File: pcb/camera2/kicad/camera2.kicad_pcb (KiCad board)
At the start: 4 copper layers, 96.5 x 45.7 mm, 71 parts

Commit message: DRC passes
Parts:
- removed the B10C at (146.4, 92.6)
- removed the B11C at (149.6, 72.3)
- removed the B15C at (153.1, 72.3)
- removed the B16C at (152.5, 67.3)
- removed the B17C at (164.4, 92.7)
- removed the B18C at (146.4, 67.3)
- removed the B19C at (166.1, 88.5)
- removed the B1C at (120.0, 88.3)
- removed the B20C at (149.9, 70.8)
- removed the B2C at (132.8, 91.7)
- removed the B3C at (153.3, 70.7)
- removed the B4C at (156.6, 70.3)
- removed the B5C at (146.5, 69.0)
- removed the B6C at (146.1, 70.5)
- removed D0C, D1C, D2C, D3C, L0, L1, L2, L3, U3C: , gen:14fdd466f7178f17380f48cf89da463f18b4a0e8fcfb609cb3e620722c947cd3
- removed D0R, D1R, D2R, D3R, RT: , gen:57f8f96f6e6b2a00af4539d585b2f3bdc0d73935af5ecd13a4a5208aab3df262
- removed U3: , gen:7dbf8df50efd715a448db095119b3b26608df54065546b11197adccbe633bb61
- added B10C: , gen:b8abd8cbc0b572999067c05d37fd407a90732e005a9769bc0f5d9b36d5f7537a, B.Cu at (146.4, 92.6)
- added B11C: , gen:b8abd8cbc0b572999067c05d37fd407a90732e005a9769bc0f5d9b36d5f7537a, B.Cu at (155.3, 91.9)
- added B15C: , gen:b8abd8cbc0b572999067c05d37fd407a90732e005a9769bc0f5d9b36d5f7537a, B.Cu at (164.1, 98.0)
- added B16C: , gen:b8abd8cbc0b572999067c05d37fd407a90732e005a9769bc0f5d9b36d5f7537a, B.Cu at (160.0, 91.0)
- added B17C: , gen:b8abd8cbc0b572999067c05d37fd407a90732e005a9769bc0f5d9b36d5f7537a, B.Cu at (164.4, 92.7)
- added B18C: , gen:b8abd8cbc0b572999067c05d37fd407a90732e005a9769bc0f5d9b36d5f7537a, B.Cu at (161.6, 86.6)
- added B19C: , gen:b8abd8cbc0b572999067c05d37fd407a90732e005a9769bc0f5d9b36d5f7537a, B.Cu at (166.1, 88.5)
- added B1C: , gen:b8abd8cbc0b572999067c05d37fd407a90732e005a9769bc0f5d9b36d5f7537a, B.Cu at (120.0, 88.3)
- added B20C: , gen:b8abd8cbc0b572999067c05d37fd407a90732e005a9769bc0f5d9b36d5f7537a, B.Cu at (180.7, 89.4)
- added B2C: , gen:b8abd8cbc0b572999067c05d37fd407a90732e005a9769bc0f5d9b36d5f7537a, B.Cu at (134.7, 90.3)
- added B3C: , gen:b8abd8cbc0b572999067c05d37fd407a90732e005a9769bc0f5d9b36d5f7537a, B.Cu at (140.1, 87.0)
- added B4C: , gen:b8abd8cbc0b572999067c05d37fd407a90732e005a9769bc0f5d9b36d5f7537a, B.Cu at (137.4, 93.0)
- added B5C: , gen:b8abd8cbc0b572999067c05d37fd407a90732e005a9769bc0f5d9b36d5f7537a, B.Cu at (142.8, 89.9)
- added B6C: , gen:b8abd8cbc0b572999067c05d37fd407a90732e005a9769bc0f5d9b36d5f7537a, B.Cu at (140.2, 95.8)
- added ID0C: , gen:b8abd8cbc0b572999067c05d37fd407a90732e005a9769bc0f5d9b36d5f7537a, B.Cu at (147.1, 118.2)
- added ID0R: , gen:8b8e8cdd2a6c07e3e6c854f6b6a8f0d2287e4fa4909b824e776fd2ffcb4b4dd2, F.Cu at (150.7, 118.2)
- added ID1C: , gen:b8abd8cbc0b572999067c05d37fd407a90732e005a9769bc0f5d9b36d5f7537a, B.Cu at (147.3, 119.2)
- added ID1R: , gen:8b8e8cdd2a6c07e3e6c854f6b6a8f0d2287e4fa4909b824e776fd2ffcb4b4dd2, F.Cu at (150.8, 119.2)
- added ID2C: , gen:b8abd8cbc0b572999067c05d37fd407a90732e005a9769bc0f5d9b36d5f7537a, B.Cu at (147.1, 120.2)
- added ID2R: , gen:8b8e8cdd2a6c07e3e6c854f6b6a8f0d2287e4fa4909b824e776fd2ffcb4b4dd2, F.Cu at (150.9, 120.3)
- added ID3C: , gen:b8abd8cbc0b572999067c05d37fd407a90732e005a9769bc0f5d9b36d5f7537a, B.Cu at (147.3, 121.1)
- added ID3R: , gen:8b8e8cdd2a6c07e3e6c854f6b6a8f0d2287e4fa4909b824e776fd2ffcb4b4dd2, F.Cu at (150.9, 121.4)
- added ID4C: , gen:b8abd8cbc0b572999067c05d37fd407a90732e005a9769bc0f5d9b36d5f7537a, F.Cu at (155.4, 118.0)
- added ID5C: , gen:b8abd8cbc0b572999067c05d37fd407a90732e005a9769bc0f5d9b36d5f7537a, F.Cu at (155.3, 119.1)
- added ID6C: , gen:b8abd8cbc0b572999067c05d37fd407a90732e005a9769bc0f5d9b36d5f7537a, F.Cu at (155.5, 120.2)
- added ID7C: , gen:b8abd8cbc0b572999067c05d37fd407a90732e005a9769bc0f5d9b36d5f7537a, F.Cu at (155.5, 121.3)
- added IL0: , gen:5ee2e2daf856c7b57c8b813aab30cc4a712b0ba6b927f36d7f82f0d8799f116d, B.Cu at (149.8, 116.5)
- added IL1: , gen:5ee2e2daf856c7b57c8b813aab30cc4a712b0ba6b927f36d7f82f0d8799f116d, B.Cu at (150.8, 116.5)
- added IL2: , gen:5ee2e2daf856c7b57c8b813aab30cc4a712b0ba6b927f36d7f82f0d8799f116d, B.Cu at (151.9, 116.5)
- added IL3: , gen:5ee2e2daf856c7b57c8b813aab30cc4a712b0ba6b927f36d7f82f0d8799f116d, B.Cu at (153.0, 116.5)
- added IR1: , gen:8b8e8cdd2a6c07e3e6c854f6b6a8f0d2287e4fa4909b824e776fd2ffcb4b4dd2, F.Cu at (159.0, 112.3)
- added IR2: , gen:8b8e8cdd2a6c07e3e6c854f6b6a8f0d2287e4fa4909b824e776fd2ffcb4b4dd2, F.Cu at (159.2, 114.0)
- added IRT: , gen:8b8e8cdd2a6c07e3e6c854f6b6a8f0d2287e4fa4909b824e776fd2ffcb4b4dd2, B.Cu at (151.1, 107.4)
- added IU3: , gen:72d1805f8915362f91f0e14214fca19b3aed8f32e64a953ec1b58a37910379a2, B.Cu at (151.4, 111.9)
- added IU3C: , gen:b8abd8cbc0b572999067c05d37fd407a90732e005a9769bc0f5d9b36d5f7537a, B.Cu at (145.8, 113.0)
- B1, B10, B11, B15, B16, B17, B18, B19, B2, B20, B3, B4, B5, B6: footprint gen:b84940fdfb16a2d7942b3b406dd98b10c2c2213999c6866e353299b244b8fc6e -> gen:bff32cade4af0a95ca028e7527e650a4e6c1ba088b705a33382b7ae8c82c305d
- C1: footprint gen:576178f3c780c7e887b8d2770ad844677200359bd7336c4d76e786b1bd821a08 -> gen:b8abd8cbc0b572999067c05d37fd407a90732e005a9769bc0f5d9b36d5f7537a
- C1M1, C2M1: footprint gen:65e19b3f16ad4d4d8558c7978771f760d319ed626d2efc1485c23fcec7e6c7b6 -> gen:4d59d39d10787b911058ae9333354a532030edea4cb4e53179d64fabcbdb6f99
- C1R1, C1R2, C2R1, C2R2, R2: footprint gen:57f8f96f6e6b2a00af4539d585b2f3bdc0d73935af5ecd13a4a5208aab3df262 -> gen:8b8e8cdd2a6c07e3e6c854f6b6a8f0d2287e4fa4909b824e776fd2ffcb4b4dd2
- C1U1, C2U1: footprint gen:d5f9e289ee2336b21afcfae927cf410e4925b1050bf518abb5cf178e2b219273 -> gen:2784497294436a743af50a5d521ce1181bd153dedc4157f9addccb1934030dc3
- C2: footprint gen:14fdd466f7178f17380f48cf89da463f18b4a0e8fcfb609cb3e620722c947cd3 -> gen:96d8d9f3b01e3a213437eecc57d99723256313ff0fc11d8291488d1af641475f
- P1: footprint gen:3c3694fa26875b1e02c9ec8a97da8ee5419b5448db42b56d2f0a8391397f0416 -> gen:3f8ed9d7be0e74029e88378a59fbf78c1191c3dbd4709bec51884f93e57b519c
- REG0: footprint gen:1add349ebd9963d752faf6d62c14ce67e4cb2b1431c56764e8a0fc8115b29539 -> gen:33f05abcc9f1c63f6620fa979925c1be2170a0d935dd6266c3361443b1a0b93c
- REG1: footprint gen:301270a8d4f2b83b7524f9f1e316186f15d4407ffff898fc97f7a9bf814ba95e -> gen:19207bd7838306c4c523d784bf9550b872fb808274892b7f9326e1c601df3f52
- REG2: footprint gen:3dff63c1257816c390bd930d4e9e2a3d002c3804d7440e0068ce39245183ded9 -> gen:d2318dfe08ea0e31695b166a9aadcf0dc3f3257fb96d848578f4303faa6cf295
- REG3: footprint gen:fab45f821aaed4b2e2c106769317244450312030644283560206288729765279 -> gen:349ed32a726ad85c4c2a09d1be6ab027e3173327b7b9892fb1b4a9c1a6d5effb
- U1: footprint gen:0306e6b5f641219b29c97fb93a4bb6fb11c91cc1b6f63197c18a4913509fb757 -> gen:07f267ebbbba037e2ec6e358fcf8ea4347767a42bf146607db79b5699d1f6bbc
- U2: footprint gen:2b1b8886a1ea8f37823178f4470ad8a0f26e8cdd6924e7ac0c0e142e2d1baa6b -> gen:37c349b4ccef9ca1e6dfa7e726c437006c67516ca70700a0b276a014844c8cb2
- moved C1 7.46 mm to (212.7, 90.4)
- moved B15 5.05 mm to (165.6, 101.0)
- moved B16 2.42 mm to (161.7, 94.2)
- moved REG3 0.45 mm to (161.6, 119.3)
- moved REG1 0.41 mm to (141.4, 119.7)
- moved REG2 0.34 mm to (162.0, 104.4)
- renumbered D0 to ID0, D1 to ID1, D2 to ID2, D3 to ID3
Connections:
- net B10_1_NC renamed _B10_1_NC
- net B10_4_NC renamed _B10_4_NC
- net B10_5_NC renamed _B10_5_NC
- net B11_1_NC renamed _B11_1_NC
- net B11_4_NC renamed _B11_4_NC
- net B11_5_NC renamed _B11_5_NC
- net B15_1_NC renamed _B15_1_NC
- net B15_4_NC renamed _B15_4_NC
- net B15_5_NC renamed _B15_5_NC
- net B16_1_NC renamed _B16_1_NC
- net B16_4_NC renamed _B16_4_NC
- net B16_5_NC renamed _B16_5_NC
- net B17_1_NC renamed _B17_1_NC
- net B17_4_NC renamed _B17_4_NC
- net B17_5_NC renamed _B17_5_NC
- net B18_1_NC renamed _B18_1_NC
- net B18_4_NC renamed _B18_4_NC
- net B18_5_NC renamed _B18_5_NC
- net B19_1_NC renamed _B19_1_NC
- net B19_4_NC renamed _B19_4_NC
- net B19_5_NC renamed _B19_5_NC
- net B1_1_NC renamed _B1_1_NC
- net B1_4_NC renamed _B1_4_NC
- net B1_5_NC renamed _B1_5_NC
- net B20_1_NC renamed _B20_1_NC
- net B20_4_NC renamed _B20_4_NC
- net B20_5_NC renamed _B20_5_NC
- net B2_1_NC renamed _B2_1_NC
- net B2_4_NC renamed _B2_4_NC
- net B2_5_NC renamed _B2_5_NC
- net B3_1_NC renamed _B3_1_NC
- net B3_4_NC renamed _B3_4_NC
- net B3_5_NC renamed _B3_5_NC
- net B4_1_NC renamed _B4_1_NC
- net B4_4_NC renamed _B4_4_NC
- net B4_5_NC renamed _B4_5_NC
- net B5_1_NC renamed _B5_1_NC
- net B5_4_NC renamed _B5_4_NC
- net B5_5_NC renamed _B5_5_NC
- net B6_1_NC renamed _B6_1_NC
- net B6_4_NC renamed _B6_4_NC
- net B6_5_NC renamed _B6_5_NC
- net REG0_4_NC renamed _REG0_4_NC
- net REG1_4_NC renamed _REG1_4_NC
- net REG2_4_NC renamed _REG2_4_NC
- net REG3_4_NC renamed _REG3_4_NC
- net T1U_17_NC renamed _T1U_17_NC
- net T1U_28_MIPI_CLK_N renamed _T1U_28_MIPI_CLK_N
- net T1U_29_MIPI_CLK_P renamed _T1U_29_MIPI_CLK_P
- net T1U_2_GPIO3 renamed _T1U_2_GPIO3
- net T1U_31_MIPI_DATA_N renamed _T1U_31_MIPI_DATA_N
- net T1U_32_MIPI_DATA_P renamed _T1U_32_MIPI_DATA_P
- net T1U_3_GPIO2 renamed _T1U_3_GPIO2
- net T1U_4_GPIO1 renamed _T1U_4_GPIO1
- net T1U_5_GPIO0 renamed _T1U_5_GPIO0
- net T2U_17_NC renamed _T2U_17_NC
- net T2U_28_MIPI_CLK_N renamed _T2U_28_MIPI_CLK_N
- net T2U_29_MIPI_CLK_P renamed _T2U_29_MIPI_CLK_P
- net T2U_2_GPIO3 renamed _T2U_2_GPIO3
- net T2U_31_MIPI_DATA_N renamed _T2U_31_MIPI_DATA_N
- net T2U_32_MIPI_DATA_P renamed _T2U_32_MIPI_DATA_P
- net T2U_3_GPIO2 renamed _T2U_3_GPIO2
- net T2U_4_GPIO1 renamed _T2U_4_GPIO1
- net T2U_5_GPIO0 renamed _T2U_5_GPIO0
- net U1_10_PA3 renamed _U1_10_PA3
- net U1_11_PA4 renamed _U1_11_PA4
- net U1_12_PA5 renamed _U1_12_PA5
- net U1_13_PA6 renamed _U1_13_PA6
- net U1_14_PA7 renamed _U1_14_PA7
- net U1_15_PB0 renamed _U1_15_PB0
- net U1_16_PB1 renamed _U1_16_PB1
- net U1_17_PB2 renamed _U1_17_PB2
- net U1_20_PA8 renamed _U1_20_PA8
- net U1_21_PA9 renamed _U1_21_PA9
- net U1_22_PA10 renamed _U1_22_PA10
- net U1_23_PA11 renamed _U1_23_PA11
- net U1_24_PA12 renamed _U1_24_PA12
- net U1_2_PD0 renamed _U1_2_PD0
- net U1_32_PB5 renamed _U1_32_PB5
- net U1_33_PB6 renamed _U1_33_PB6
- net U1_34_PB7 renamed _U1_34_PB7
- net U1_3_PD1 renamed _U1_3_PD1
- net U1_5_VSSA renamed _U1_5_VSSA
- net U1_6_VDDA renamed _U1_6_VDDA
- net U1_7_PA0 renamed _U1_7_PA0
- net U1_8_PA1 renamed _U1_8_PA1
- net U1_9_PA2 renamed _U1_9_PA2
- net U2_10_IO2_10 renamed _U2_10_IO2_10
- net U2_11_IO2_11 renamed _U2_11_IO2_11
- net U2_1_IO2_1 renamed _U2_1_IO2_1
- net U2_2_IO2_2 renamed _U2_2_IO2_2
- net U2_3_IO2_3 renamed _U2_3_IO2_3
- net U2_4_IO2_4 renamed _U2_4_IO2_4
- net U2_53_IO1_53 renamed _U2_53_IO1_53
- net U2_54_IO1_54 renamed _U2_54_IO1_54
- net U2_55_IO1_55 renamed _U2_55_IO1_55
- net U2_56_IO1_56 renamed _U2_56_IO1_56
- net U2_58_IO1_58 renamed _U2_58_IO1_58
- net U2_59_IO1_59 renamed _U2_59_IO1_59
- net U2_60_IO1_60 renamed _U2_60_IO1_60
- net U2_61_IO1_61 renamed _U2_61_IO1_61
- net U2_63_IO1_63 renamed _U2_63_IO1_63
- net U2_64_IO1_64 renamed _U2_64_IO1_64
- net U2_65_IO2_65 renamed _U2_65_IO2_65
- net U2_66_IO2_66 renamed _U2_66_IO2_66
- net U2_67_IO2_67 renamed _U2_67_IO2_67
- net U2_68_IO2_68 renamed _U2_68_IO2_68
- net U2_6_IO2_6 renamed _U2_6_IO2_6
- net U2_70_IO2_70 renamed _U2_70_IO2_70
- net U2_71_IO2_71 renamed _U2_71_IO2_71
- net U2_72_IO2_72 renamed _U2_72_IO2_72
- net U2_73_IO2_73 renamed _U2_73_IO2_73
- net U2_74_IO2_74 renamed _U2_74_IO2_74
- net U2_76_IO2_76 renamed _U2_76_IO2_76
- net U2_7_IO2_7 renamed _U2_7_IO2_7
- net U2_8_IO2_8 renamed _U2_8_IO2_8
- net U2_9_IO2_9 renamed _U2_9_IO2_9
- ID0 pad 1: cat0 -> Icat0
- ID0 pad 2: led0 -> Iled0
- ID1 pad 1: cat1 -> Icat1
- ID1 pad 2: led1 -> Iled1
- ID2 pad 1: cat2 -> Icat2
- ID2 pad 2: led2 -> Iled2
- ID3 pad 1: cat3 -> Icat3
- ID3 pad 2: led3 -> Iled3
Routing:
- net vcc3_0: track 4.31 -> 14.1 mm, vias 5 -> 14
- net gnd: track 30.7 -> 39.5 mm, vias 31 -> 43
- net pair15P: track 14.2 -> 19.3 mm
- net pair15N: track 17.2 -> 22.3 mm
- net out15P: track 30.7 -> 25.7 mm
- net out15N: track 31.0 -> 26.0 mm
- net vcc1_8: track 2.17 -> 5.21 mm, vias 2 -> 5
- net pair16N: track 10.8 -> 13.2 mm
- net pair16P: track 7.80 -> 10.3 mm
- net out16P: track 34.3 -> 31.9 mm
- net out16N: track 34.6 -> 32.2 mm
- net vcc3_3in: track 6.71 -> 6.12 mm, vias 2 -> 1
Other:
- rule pad_to_mask_clearance: 0.2 -> 0
- board text added: "1.8"

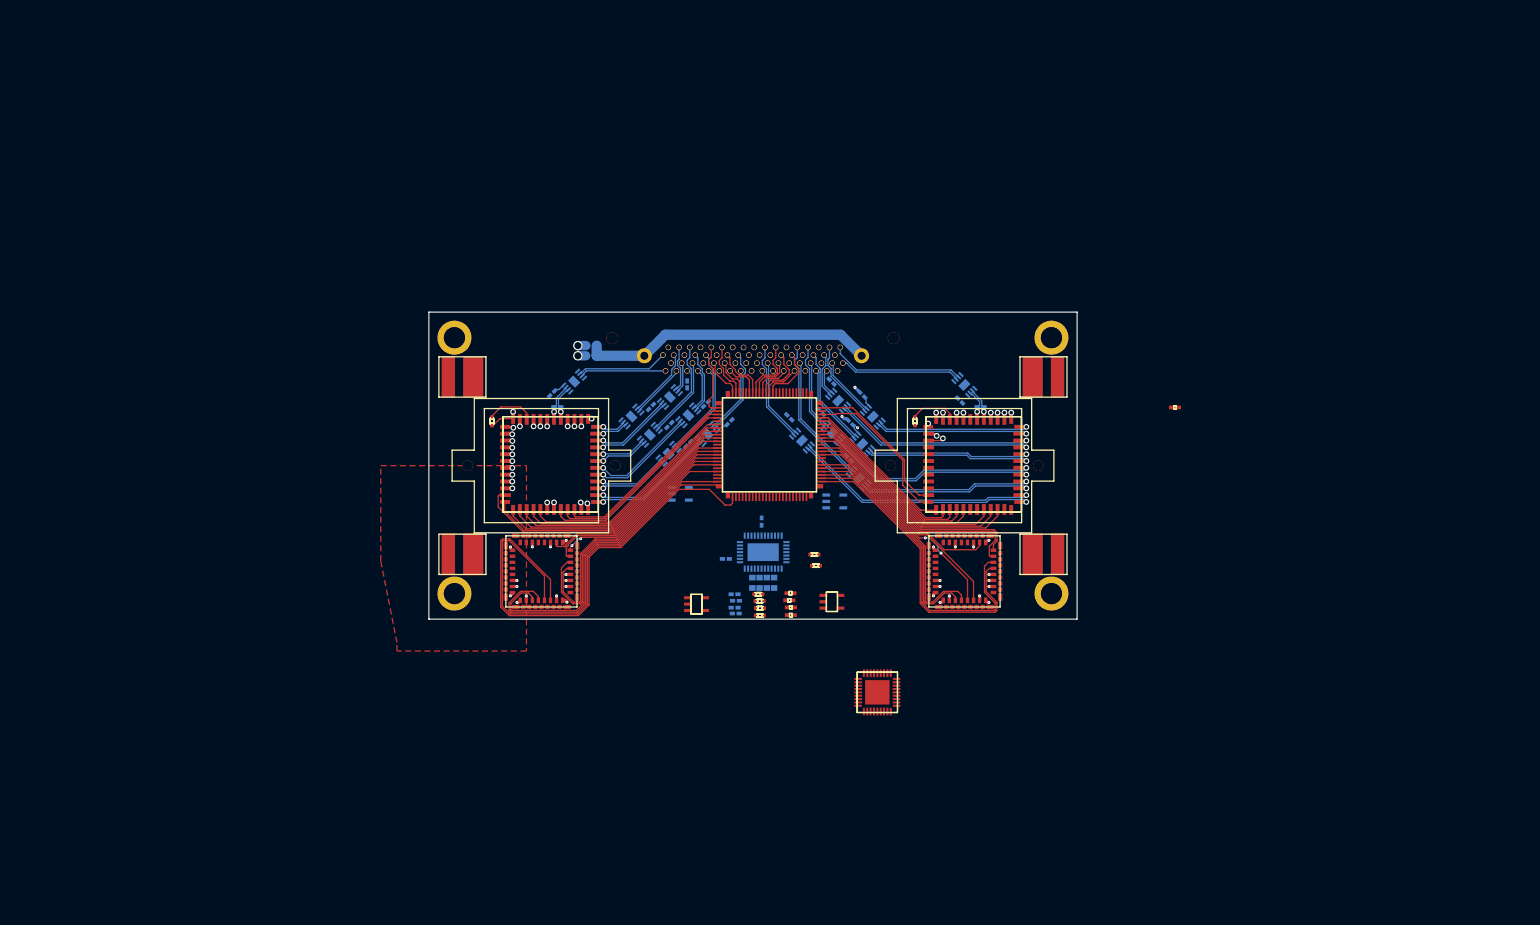
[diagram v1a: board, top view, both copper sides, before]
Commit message: adding decoupling capacitors
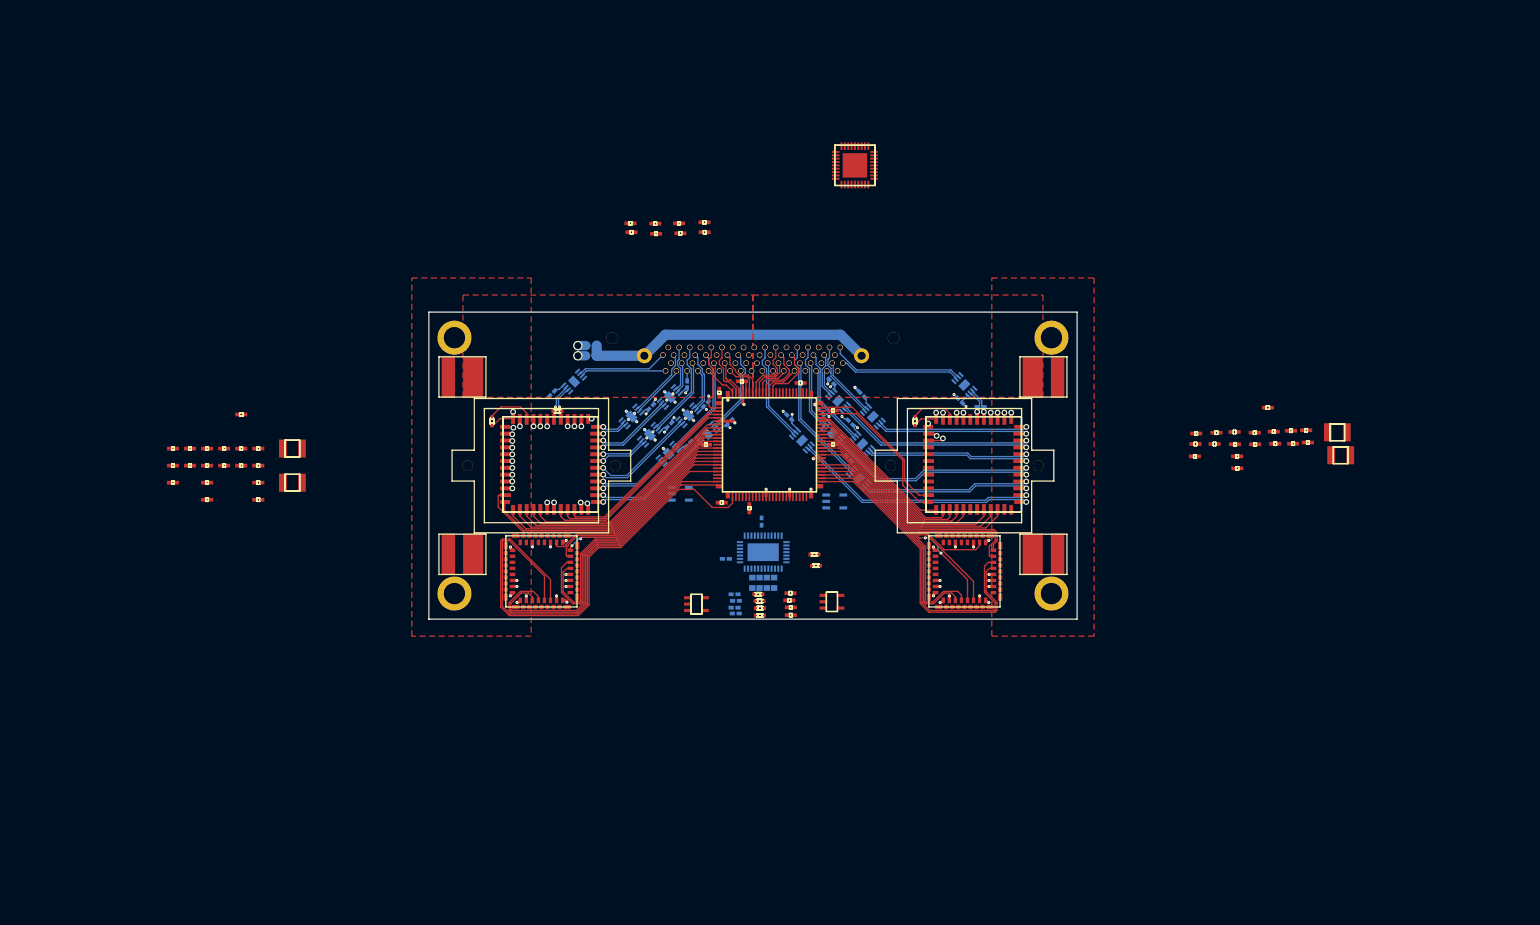
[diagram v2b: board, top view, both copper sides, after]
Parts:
- removed C1: , gen:b8abd8cbc0b572999067c05d37fd407a90732e005a9769bc0f5d9b36d5f7537a
- removed U1: , gen:07f267ebbbba037e2ec6e358fcf8ea4347767a42bf146607db79b5699d1f6bbc
- added C1C10: , gen:b8abd8cbc0b572999067c05d37fd407a90732e005a9769bc0f5d9b36d5f7537a, F.Cu at (63.5, 96.5)
- added C1C11: , gen:b8abd8cbc0b572999067c05d37fd407a90732e005a9769bc0f5d9b36d5f7537a, F.Cu at (63.5, 99.1)
- added C1C12: , gen:b8abd8cbc0b572999067c05d37fd407a90732e005a9769bc0f5d9b36d5f7537a, F.Cu at (63.5, 101.6)
- added C1C20: , gen:b8abd8cbc0b572999067c05d37fd407a90732e005a9769bc0f5d9b36d5f7537a, F.Cu at (66.0, 96.5)
- added C1C21: , gen:b8abd8cbc0b572999067c05d37fd407a90732e005a9769bc0f5d9b36d5f7537a, F.Cu at (66.0, 99.1)
- added C1C30: , gen:b8abd8cbc0b572999067c05d37fd407a90732e005a9769bc0f5d9b36d5f7537a, F.Cu at (68.6, 96.5)
- added C1C31: , gen:b8abd8cbc0b572999067c05d37fd407a90732e005a9769bc0f5d9b36d5f7537a, F.Cu at (68.6, 99.1)
- added C1C32: , gen:b8abd8cbc0b572999067c05d37fd407a90732e005a9769bc0f5d9b36d5f7537a, F.Cu at (68.6, 101.6)
- added C1C33: , gen:b8abd8cbc0b572999067c05d37fd407a90732e005a9769bc0f5d9b36d5f7537a, F.Cu at (68.6, 104.1)
- added C1C40: , gen:b8abd8cbc0b572999067c05d37fd407a90732e005a9769bc0f5d9b36d5f7537a, F.Cu at (71.1, 96.5)
- added C1C41: , gen:b8abd8cbc0b572999067c05d37fd407a90732e005a9769bc0f5d9b36d5f7537a, F.Cu at (71.1, 99.1)
- added C1C50: , gen:b8abd8cbc0b572999067c05d37fd407a90732e005a9769bc0f5d9b36d5f7537a, F.Cu at (73.7, 96.5)
- added C1C51: , gen:b8abd8cbc0b572999067c05d37fd407a90732e005a9769bc0f5d9b36d5f7537a, F.Cu at (73.7, 99.1)
- added C1C60: , gen:b8abd8cbc0b572999067c05d37fd407a90732e005a9769bc0f5d9b36d5f7537a, F.Cu at (76.2, 96.5)
- added C1C61: , gen:b8abd8cbc0b572999067c05d37fd407a90732e005a9769bc0f5d9b36d5f7537a, F.Cu at (76.2, 99.1)
- added C1C62: , gen:b8abd8cbc0b572999067c05d37fd407a90732e005a9769bc0f5d9b36d5f7537a, F.Cu at (76.2, 101.6)
- added C1C63: , gen:b8abd8cbc0b572999067c05d37fd407a90732e005a9769bc0f5d9b36d5f7537a, F.Cu at (76.2, 104.1)
- added C1C70: , gen:2dd82497e3d208e8bc654e5fd2889726ca886e84a8d673bd1d967596710ae728, F.Cu at (81.3, 96.5)
- added C1C71: , gen:2dd82497e3d208e8bc654e5fd2889726ca886e84a8d673bd1d967596710ae728, F.Cu at (81.3, 101.6)
- added C1FB1: , gen:4c7c45a8243ee1f12f8b92439e457e230f10814780b518cd649ab5c65f1663b6, F.Cu at (73.7, 91.4)
- added C2C10: , gen:b8abd8cbc0b572999067c05d37fd407a90732e005a9769bc0f5d9b36d5f7537a, F.Cu at (215.9, 94.3)
- added C2C11: , gen:b8abd8cbc0b572999067c05d37fd407a90732e005a9769bc0f5d9b36d5f7537a, F.Cu at (215.8, 95.8)
- added C2C12: , gen:b8abd8cbc0b572999067c05d37fd407a90732e005a9769bc0f5d9b36d5f7537a, F.Cu at (215.7, 97.7)
- added C2C20: , gen:b8abd8cbc0b572999067c05d37fd407a90732e005a9769bc0f5d9b36d5f7537a, F.Cu at (218.9, 94.2)
- added C2C21: , gen:b8abd8cbc0b572999067c05d37fd407a90732e005a9769bc0f5d9b36d5f7537a, F.Cu at (218.6, 95.8)
- added C2C30: , gen:b8abd8cbc0b572999067c05d37fd407a90732e005a9769bc0f5d9b36d5f7537a, F.Cu at (221.6, 94.0)
- added C2C31: , gen:b8abd8cbc0b572999067c05d37fd407a90732e005a9769bc0f5d9b36d5f7537a, F.Cu at (221.7, 95.9)
- added C2C32: , gen:b8abd8cbc0b572999067c05d37fd407a90732e005a9769bc0f5d9b36d5f7537a, F.Cu at (222.0, 97.7)
- added C2C33: , gen:b8abd8cbc0b572999067c05d37fd407a90732e005a9769bc0f5d9b36d5f7537a, F.Cu at (222.0, 99.5)
- added C2C40: , gen:b8abd8cbc0b572999067c05d37fd407a90732e005a9769bc0f5d9b36d5f7537a, F.Cu at (224.6, 94.2)
- added C2C41: , gen:b8abd8cbc0b572999067c05d37fd407a90732e005a9769bc0f5d9b36d5f7537a, F.Cu at (224.6, 95.9)
- added C2C50: , gen:b8abd8cbc0b572999067c05d37fd407a90732e005a9769bc0f5d9b36d5f7537a, F.Cu at (227.4, 94.0)
- added C2C51: , gen:b8abd8cbc0b572999067c05d37fd407a90732e005a9769bc0f5d9b36d5f7537a, F.Cu at (227.6, 95.8)
- added C2C60: , gen:b8abd8cbc0b572999067c05d37fd407a90732e005a9769bc0f5d9b36d5f7537a, F.Cu at (230.0, 93.9)
- added C2C61: , gen:b8abd8cbc0b572999067c05d37fd407a90732e005a9769bc0f5d9b36d5f7537a, F.Cu at (230.3, 95.8)
- added C2C62: , gen:b8abd8cbc0b572999067c05d37fd407a90732e005a9769bc0f5d9b36d5f7537a, F.Cu at (232.2, 93.8)
- added C2C63: , gen:b8abd8cbc0b572999067c05d37fd407a90732e005a9769bc0f5d9b36d5f7537a, F.Cu at (232.5, 95.6)
- added C2C70: , gen:2dd82497e3d208e8bc654e5fd2889726ca886e84a8d673bd1d967596710ae728, F.Cu at (236.9, 94.1)
- added C2C71: , gen:2dd82497e3d208e8bc654e5fd2889726ca886e84a8d673bd1d967596710ae728, F.Cu at (237.4, 97.5)
- added C2FB1: , gen:4c7c45a8243ee1f12f8b92439e457e230f10814780b518cd649ab5c65f1663b6, F.Cu at (226.5, 90.4)
- added MU1: , gen:367b1dfe5fbef908783f66763bd7a5acf5e4e9ac323dc2ecd365e9480193a983, F.Cu at (165.0, 54.4)
- added REG0C1: , gen:b8abd8cbc0b572999067c05d37fd407a90732e005a9769bc0f5d9b36d5f7537a, F.Cu at (131.6, 63.0)
- added REG0C2: , gen:b8abd8cbc0b572999067c05d37fd407a90732e005a9769bc0f5d9b36d5f7537a, F.Cu at (131.8, 64.3)
- added REG1C1: , gen:b8abd8cbc0b572999067c05d37fd407a90732e005a9769bc0f5d9b36d5f7537a, F.Cu at (135.3, 63.0)
- added REG1C2: , gen:b8abd8cbc0b572999067c05d37fd407a90732e005a9769bc0f5d9b36d5f7537a, F.Cu at (135.4, 64.5)
- added REG2C1: , gen:b8abd8cbc0b572999067c05d37fd407a90732e005a9769bc0f5d9b36d5f7537a, F.Cu at (138.9, 63.0)
- added REG2C2: , gen:b8abd8cbc0b572999067c05d37fd407a90732e005a9769bc0f5d9b36d5f7537a, F.Cu at (139.1, 64.5)
- added REG3C1: , gen:b8abd8cbc0b572999067c05d37fd407a90732e005a9769bc0f5d9b36d5f7537a, F.Cu at (142.6, 62.8)
- added REG3C2: , gen:b8abd8cbc0b572999067c05d37fd407a90732e005a9769bc0f5d9b36d5f7537a, F.Cu at (142.7, 64.3)
- added U2C0: , gen:b8abd8cbc0b572999067c05d37fd407a90732e005a9769bc0f5d9b36d5f7537a, F.Cu at (148.2, 86.5)
- added U2C1: , gen:b8abd8cbc0b572999067c05d37fd407a90732e005a9769bc0f5d9b36d5f7537a, F.Cu at (142.8, 96.0)
- added U2C10: , gen:b8abd8cbc0b572999067c05d37fd407a90732e005a9769bc0f5d9b36d5f7537a, F.Cu at (149.3, 105.4)
- added U2C11: , gen:b8abd8cbc0b572999067c05d37fd407a90732e005a9769bc0f5d9b36d5f7537a, F.Cu at (144.8, 88.2)
- added U2C2: , gen:b8abd8cbc0b572999067c05d37fd407a90732e005a9769bc0f5d9b36d5f7537a, F.Cu at (156.9, 86.8)
- added U2C3: , gen:b8abd8cbc0b572999067c05d37fd407a90732e005a9769bc0f5d9b36d5f7537a, F.Cu at (145.2, 104.6)
- added U2C4: , gen:b8abd8cbc0b572999067c05d37fd407a90732e005a9769bc0f5d9b36d5f7537a, F.Cu at (161.8, 95.9)
- added U2C5: , gen:b8abd8cbc0b572999067c05d37fd407a90732e005a9769bc0f5d9b36d5f7537a, F.Cu at (161.8, 90.8)
- B1, B10, B11, B15, B16, B17, B18, B19, B2, B20, B3, B4, B5, B6: footprint gen:bff32cade4af0a95ca028e7527e650a4e6c1ba088b705a33382b7ae8c82c305d -> gen:c10439afd0d8b6257ef1c27f4f82fc58c3d4c5054283b74b6b66a4104acdf316
- C1R2: moved to F.Cu
- C1U1, C2U1: footprint gen:2784497294436a743af50a5d521ce1181bd153dedc4157f9addccb1934030dc3 -> gen:b63fcc5f9d3775f8fe70cf3fb5d8b5f04a7eca08ac47608b5e89638e98bcb700
- IU3: footprint gen:72d1805f8915362f91f0e14214fca19b3aed8f32e64a953ec1b58a37910379a2 -> gen:e3b0d12270c7c85838eec4ea49236d406538843f4d15834af3fc0cb77d220f02
- REG0: footprint gen:33f05abcc9f1c63f6620fa979925c1be2170a0d935dd6266c3361443b1a0b93c -> gen:3d99036cd480df3a971e9332a10991f4b4057d7616fab2d4316ebb8abf971d82
- REG1: footprint gen:19207bd7838306c4c523d784bf9550b872fb808274892b7f9326e1c601df3f52 -> gen:75dc3698b1ff6542e4f243061f87141af8b001abff0d9b87a3453e35e9a44ae7
- REG2: footprint gen:d2318dfe08ea0e31695b166a9aadcf0dc3f3257fb96d848578f4303faa6cf295 -> gen:5c5735648a39745ab185332e5d476d2f8d0f0732e4cbb77a264faa59f1279769
- REG3: footprint gen:349ed32a726ad85c4c2a09d1be6ab027e3173327b7b9892fb1b4a9c1a6d5effb -> gen:56154983e65433cbe4274fc9c6e8546888a42988748c6bed8e94b66f0094f817
- moved C1R2 0.64 mm to (120.8, 91.0)
- moved M0 0.63 mm to (105.4, 80.0)
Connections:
- C1U1 pad 31: vcc3_0 -> C1vdd_pix
- C1U1 pad 33: vcc3_0 -> C1vdd_pix
- C1U1 pad 38: vcc3_0 -> C1vdd_pix
- C1U1 pad 40: vcc3_0 -> C1vdd_pix
- C2U1 pad 31: vcc3_0 -> C2vdd_pix
- C2U1 pad 33: vcc3_0 -> C2vdd_pix
- C2U1 pad 38: vcc3_0 -> C2vdd_pix
- C2U1 pad 40: vcc3_0 -> C2vdd_pix
- REG0 pad 5: vcc1_2 -> vcc1_8
- REG1 pad 5: vcc1_8 -> vcc3_0
- REG2 pad 5: vcc3_0 -> vcc1_2
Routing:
- net gnd: track 39.5 -> 78.5 mm, vias 43 -> 74
- net vcc3_3in: track 6.12 -> 25.4 mm, vias 1 -> 10
- net vcc3_0: track 14.1 -> 8.77 mm, vias 14 -> 8
- net C1vdd_pix: track 0.00 -> 4.38 mm, vias 0 -> 4
- net C2vdd_pix: track 0.00 -> 2.74 mm, vias 0 -> 2
- net out1N: track 6.27 -> 5.55 mm
- net out1P: track 6.00 -> 5.29 mm
- added copper zone on F.Cu, net Iled0
- added copper zone on F.Cu, net Iled1
- added copper zone on F.Cu, net Iled2
- added copper zone on F.Cu, net Iled3
- added copper zone on In1.Cu, net vcc3_0
- removed copper zone on F.Cu, net D1_2_A
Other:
- board text added: "move CPLD down so that horizontal traces have to travel minimally"

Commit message: camera pcb work
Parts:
- added D0U: , gen:cfb627babe9c1af1f33c85d37ce6deca4dd211aac43cd0425c7aedd41ca50871, F.Cu at (113.3, 84.3)
- added D1U: , gen:cfb627babe9c1af1f33c85d37ce6deca4dd211aac43cd0425c7aedd41ca50871, F.Cu at (109.7, 118.4)
- added D2U: , gen:cfb627babe9c1af1f33c85d37ce6deca4dd211aac43cd0425c7aedd41ca50871, F.Cu at (189.7, 118.5)
- added D3U: , gen:cfb627babe9c1af1f33c85d37ce6deca4dd211aac43cd0425c7aedd41ca50871, F.Cu at (186.3, 84.1)
- added SC0: , gen:b8abd8cbc0b572999067c05d37fd407a90732e005a9769bc0f5d9b36d5f7537a, F.Cu at (74.1, 57.4)
- added SC1: , gen:b8abd8cbc0b572999067c05d37fd407a90732e005a9769bc0f5d9b36d5f7537a, F.Cu at (90.3, 62.8)
- added SC2: , gen:b8abd8cbc0b572999067c05d37fd407a90732e005a9769bc0f5d9b36d5f7537a, F.Cu at (90.6, 61.4)
- added SC3: , gen:b8abd8cbc0b572999067c05d37fd407a90732e005a9769bc0f5d9b36d5f7537a, F.Cu at (90.1, 59.7)
- added SU1: , gen:f9c3ae8e9607776eb8d584f2f53baa49589c5cbd0e39654446d2f839acd0d9d0, F.Cu at (76.9, 58.7)
- added SU2: , gen:604093d92b23f96c780cabef8c052d038c2078bb1aa740e14df8b0cb48f3327f, F.Cu at (86.6, 61.3)
- B1, B10, B11, B15, B16, B17, B18, B19, B2, B20, B3, B4, B5, B6: footprint gen:c10439afd0d8b6257ef1c27f4f82fc58c3d4c5054283b74b6b66a4104acdf316 -> gen:499eb9275f53d39e8577307f805591431933e719fae192caf99d98aedcaee8aa
- IU3: footprint gen:e3b0d12270c7c85838eec4ea49236d406538843f4d15834af3fc0cb77d220f02 -> gen:eae6644e6b99af62deb74575fada904c5eece19a089fdb5d682cd29a528e43eb
- MU1: footprint gen:367b1dfe5fbef908783f66763bd7a5acf5e4e9ac323dc2ecd365e9480193a983 -> gen:8eebdf892b6f01e0d95a0c2299292ab3ec84d1b3707fa7ee95a6b86d4bb590c8
- REG0: footprint gen:3d99036cd480df3a971e9332a10991f4b4057d7616fab2d4316ebb8abf971d82 -> gen:7b67745b4d523e87fae434cdb8f46b54d22e1bc4395fdb8e73632e915883351d
- REG1: footprint gen:75dc3698b1ff6542e4f243061f87141af8b001abff0d9b87a3453e35e9a44ae7 -> gen:798cf5bb0b3169533f5ca04ecb4ee99ae7bea0b47d3b6b0eac8ced07210df3aa
- REG2: footprint gen:5c5735648a39745ab185332e5d476d2f8d0f0732e4cbb77a264faa59f1279769 -> gen:6bc819ec539c21ef6344b6fd02be2ed3f4459069e5b504ecb87402b55c84b9f4
- REG3: footprint gen:56154983e65433cbe4274fc9c6e8546888a42988748c6bed8e94b66f0094f817 -> gen:817c1b12dae0694d00766759c3a729f1e099230e7310e0e9cf5cf1b3dbba25eb
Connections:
- REG0 pad 5: vcc1_8 -> vcc3_0
- REG0C2 pad 1: vcc1_8 -> vcc3_0
- REG1 pad 5: vcc3_0 -> vcc1_8
- REG1C2 pad 1: vcc3_0 -> vcc1_8
